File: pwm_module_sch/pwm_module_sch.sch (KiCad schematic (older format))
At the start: 47 parts, among them J1 SWIMM, J2 output -, J3 input, J4 output+, Q1 AO3400, Q2 6N60, SW1 ., SW2 ., U1 TM1637, U2 STM8S003F3P, U3 LM358, U4 L78L33

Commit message: low lewel written, not tested, todo: main menu
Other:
- moved on the sheet: C5, Q1, R4
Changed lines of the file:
@@
 L Device:R R4
 U 1 1 620AEA05
-P 4650 2800
-F 0 "R4" H 4700 2850 50  0000 L CNN
-F 1 "100k" V 4650 2700 50  0000 L CNN
-F 2 "Resistor_SMD:R_0402_1005Metric" V 4580 2800 50  0001 C CNN
-F 3 "~" H 4650 2800 50  0001 C CNN
-	1    4650 2800
-	1    0    0    -1
-$EndComp
-Wire Wire Line
-	4650 3050 4650 3000
-Connection ~ 4650 3000
-Wire Wire Line
-	4650 3000 4650 2950
+P 4700 2800
+F 0 "R4" H 4750 2850 50  0000 L CNN
+F 1 "100k" V 4700 2700 50  0000 L CNN
+F 2 "Resistor_SMD:R_0402_1005Metric" V 4630 2800 50  0001 C CNN
+F 3 "~" H 4700 2800 50  0001 C CNN
+	1    4700 2800
+	1    0    0    -1
+$EndComp
 $Comp
 L power:GND #PWR0105
@@
 	1    0    0    -1
 $EndComp
-Wire Wire Line
-	4650 3000 4950 3000
 $Comp
 L Device:R_Potentiometer RV1
@@
 	1    0    0    -1
 $EndComp
-Wire Wire Line
-	4350 2900 4350 2850
-Wire Wire Line
-	4650 2600 4650 2650
 $Comp
 L Amplifier_Operational:LM358 U3
@@
 L power:+VSW #PWR0112
 U 1 1 6218088D
-P 5200 2550
-F 0 "#PWR0112" H 5200 2400 50  0001 C CNN
-F 1 "+VSW" H 5200 2700 50  0000 C CNN
-F 2 "" H 5200 2550 50  0001 C CNN
-F 3 "" H 5200 2550 50  0001 C CNN
-	1    5200 2550
+P 5250 2550
+F 0 "#PWR0112" H 5250 2400 50  0001 C CNN
+F 1 "+VSW" H 5250 2700 50  0000 C CNN
+F 2 "" H 5250 2550 50  0001 C CNN
+F 3 "" H 5250 2550 50  0001 C CNN
+	1    5250 2550
 	1    0    0    -1
 $EndComp
@@
 L power:+24V #PWR0113
 U 1 1 6218BBB0
-P 4650 2550
-F 0 "#PWR0113" H 4650 2400 50  0001 C CNN
-F 1 "+24V" H 4650 2700 50  0000 C CNN
-F 2 "" H 4650 2550 50  0001 C CNN
-F 3 "" H 4650 2550 50  0001 C CNN
-	1    4650 2550
-	1    0    0    -1
-$EndComp
-Wire Wire Line
-	4650 2600 4650 2550
-Connection ~ 4650 2600
-Wire Wire Line
-	4750 2600 4650 2600
-Wire Wire Line
-	4950 2900 4950 3000
-Wire Wire Line
-	5150 2600 5200 2600
-Wire Wire Line
-	5200 2600 5200 2550
+P 4700 2550
+F 0 "#PWR0113" H 4700 2400 50  0001 C CNN
+F 1 "+24V" H 4700 2700 50  0000 C CNN
+F 2 "" H 4700 2550 50  0001 C CNN
+F 3 "" H 4700 2550 50  0001 C CNN
+	1    4700 2550
+	1    0    0    -1
+$EndComp
 $Comp
 L power:+3.3V #PWR0114
@@
 	1    0    0    -1
 $EndComp
-Connection ~ 5200 2600
 $Comp
 L Device:C_Polarized_US C5
 U 1 1 62166329
-P 5200 2950
-F 0 "C5" H 5200 3050 50  0000 L CNN
-F 1 "1000uF" H 4900 2850 50  0000 L CNN
-F 2 "Capacitor_THT:CP_Radial_D5.0mm_P2.00mm" H 5200 2950 50  0001 C CNN
-F 3 "~" H 5200 2950 50  0001 C CNN
-	1    5200 2950
-	1    0    0    -1
-$EndComp
-Wire Wire Line
-	5200 2800 5200 2600
+P 5250 2950
+F 0 "C5" H 5250 3050 50  0000 L CNN
+F 1 "1000uF" H 4950 2850 50  0000 L CNN
+F 2 "Capacitor_THT:CP_Radial_D5.0mm_P2.00mm" H 5250 2950 50  0001 C CNN
+F 3 "~" H 5250 2950 50  0001 C CNN
+	1    5250 2950
+	1    0    0    -1
+$EndComp
 $Comp
 L Device:R R2
@@
 Wire Wire Line
 	5300 1850 5450 1850
-Wire Wire Line
-	5450 1850 5450 2350
-Wire Wire Line
-	5450 2350 5500 2350
 Connection ~ 5300 1850
-Wire Wire Line
-	5450 2600 5450 2450
-Wire Wire Line
-	5200 2600 5450 2600
-Wire Wire Line
-	5450 2450 5500 2450
 Wire Wire Line
 	4050 1050 4100 1050
@@
 	0    1    1    0
 $EndComp
-Wire Wire Line
-	4350 3250 4350 3200
 $Comp
 L Connector_Generic:Conn_01x01 J4
@@
 L power:GND #PWR0129
 U 1 1 62235D6C
-P 5200 3550
-F 0 "#PWR0129" H 5200 3300 50  0001 C CNN
-F 1 "GND" H 5300 3450 50  0000 C CNN
-F 2 "" H 5200 3550 50  0001 C CNN
-F 3 "" H 5200 3550 50  0001 C CNN
-	1    5200 3550
+P 5250 3550
+F 0 "#PWR0129" H 5250 3300 50  0001 C CNN
+F 1 "GND" H 5350 3450 50  0000 C CNN
+F 2 "" H 5250 3550 50  0001 C CNN
+F 3 "" H 5250 3550 50  0001 C CNN
+	1    5250 3550
 	1    0    0    -1
 $EndComp
@@
 	2200 3050 2200 6250
 Wire Wire Line
-	5200 3500 5200 3100
-Wire Wire Line
 	4200 3450 4200 4650
 Wire Wire Line
-	4350 3250 4300 3250
-Wire Wire Line
 	4000 3250 3950 3250
-Wire Wire Line
-	3950 3350 4300 3350
-Wire Wire Line
-	4300 3350 4300 3900
-Connection ~ 4300 3900
-Connection ~ 4350 3250
 $Comp
 L local:AO3400 Q1
 U 1 1 620ABAF0
-P 4550 3250
-F 0 "Q1" H 4756 3296 50  0000 L CNN
-F 1 "AO3400" H 4756 3205 50  0000 L CNN
-F 2 "Package_TO_SOT_SMD:SOT-23" H 4550 3250 50  0001 C CNN
-F 3 "" H 4550 3250 50  0001 L CNN
-	1    4550 3250
-	1    0    0    -1
-$EndComp
-Wire Wire Line
-	4650 3450 4650 3500
-Wire Wire Line
-	4650 3500 5200 3500
-Wire Wire Line
-	5200 3550 5200 3500
-Connection ~ 5200 3500
+P 4600 3250
+F 0 "Q1" H 4806 3296 50  0000 L CNN
+F 1 "AO3400" H 4806 3205 50  0000 L CNN
+F 2 "Package_TO_SOT_SMD:SOT-23" H 4600 3250 50  0001 C CNN
+F 3 "" H 4600 3250 50  0001 L CNN
+	1    4600 3250
+	1    0    0    -1
+$EndComp
 $Comp
 L Device:R R11
@@
 Wire Wire Line
 	2300 5900 2300 5850
+Wire Wire Line
+	4350 3200 4350 3250
+Wire Wire Line
+	4350 3250 4400 3250
+Wire Wire Line
+	4300 3250 4350 3250
+Connection ~ 4350 3250
+Wire Wire Line
+	4350 2900 4350 2850
+Wire Wire Line
+	4700 3450 4700 3500
+Wire Wire Line
+	4950 2900 4950 3000
+Wire Wire Line
+	4950 3000 4700 3000
+Wire Wire Line
+	4700 3000 4700 3050
+Wire Wire Line
+	4700 2950 4700 3000
+Connection ~ 4700 3000
+Wire Wire Line
+	4700 2650 4700 2600
+Wire Wire Line
+	4750 2600 4700 2600
+Connection ~ 4700 2600
+Wire Wire Line
+	4700 2600 4700 2550
+Wire Wire Line
+	5150 2600 5250 2600
+Wire Wire Line
+	5250 3500 5250 3550
+Wire Wire Line
+	4700 3500 5250 3500
+Wire Wire Line
+	5250 3100 5250 3500
+Connection ~ 5250 3500
+Wire Wire Line
+	5250 2800 5250 2600
+Connection ~ 5250 2600
+Wire Wire Line
+	5250 2600 5250 2550
+Wire Wire Line
+	5450 1850 5450 2350
+Wire Wire Line
+	5450 2350 5500 2350
+Wire Wire Line
+	5250 2600 5350 2600
+Wire Wire Line
+	5350 2600 5350 2450
+Wire Wire Line
+	5350 2450 5500 2450
+Wire Wire Line
+	4300 3900 4300 3350
+Wire Wire Line
+	4300 3350 3950 3350
+Connection ~ 4300 3900
 $EndSCHEMATC

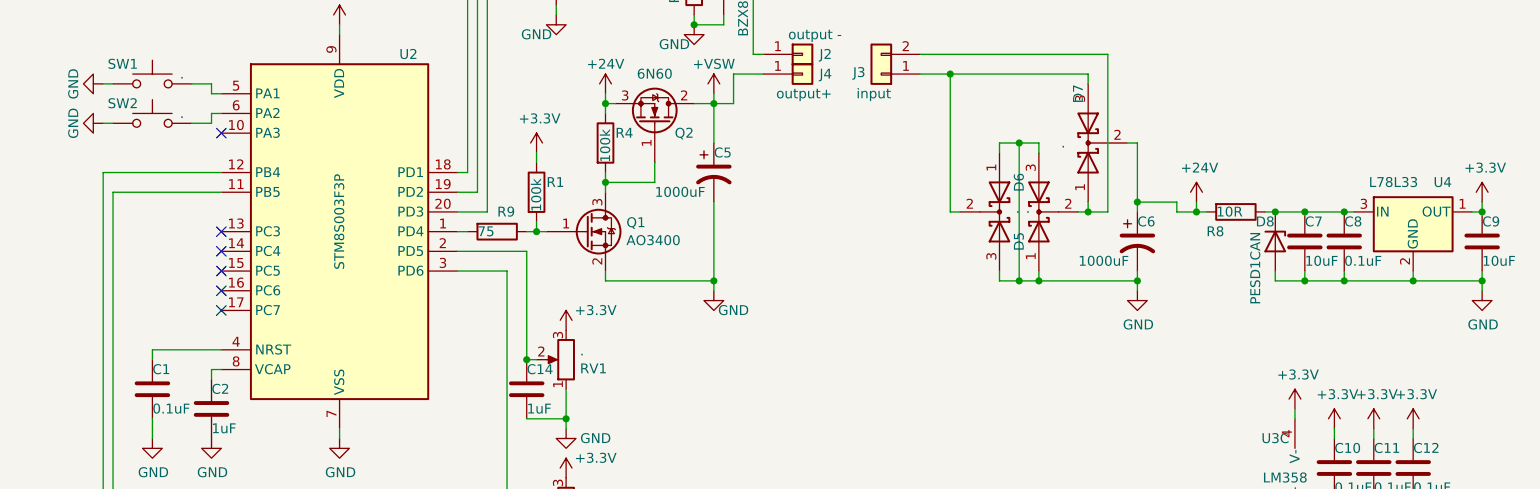
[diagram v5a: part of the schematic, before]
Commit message: uart sch add
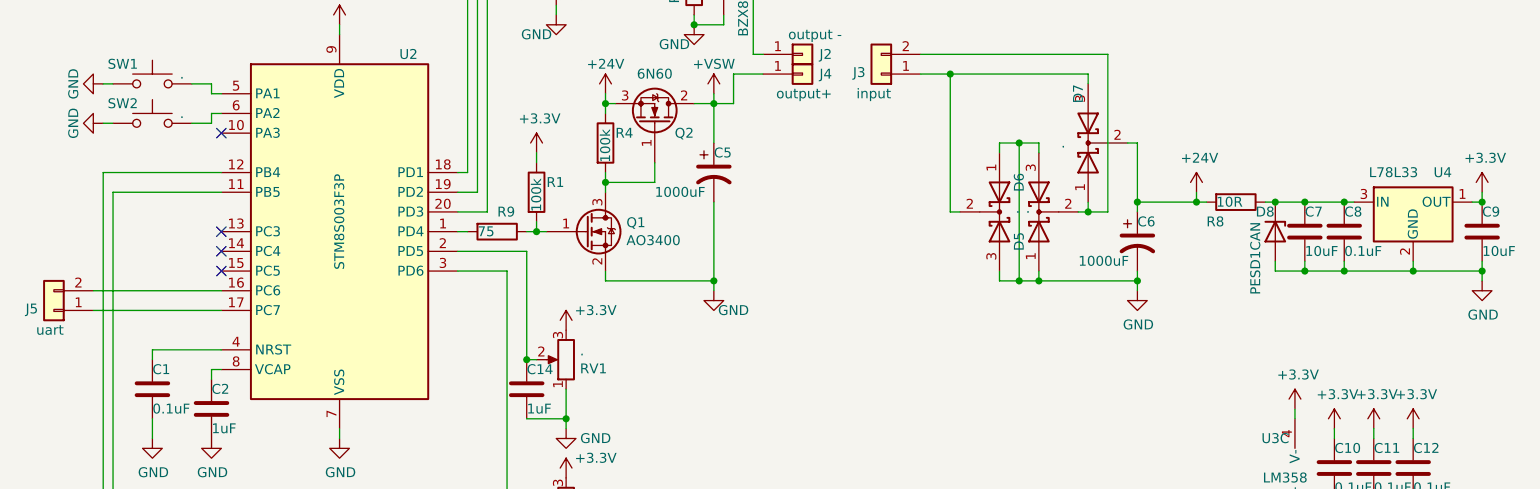
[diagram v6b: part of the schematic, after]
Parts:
- added J5: uart, Connector_PinHeader_2.54mm:PinHeader_1x02_P2.54mm_Vertical, symbol Connector_Generic:Conn_01x02
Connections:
- net at U2.16 (PC6): now also J5.2 (Pin_2)
- net at U2.17 (PC7): now also J5.1 (Pin_1)
- no-connect marks 8 -> 6
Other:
- moved on the sheet: C7, C8, C9, D8, R8, U4
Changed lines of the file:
@@
-$EndComp
-$Comp
-L Regulator_Linear:L78L33_SOT89 U4
-U 1 1 62099343
-P 8800 3150
-F 0 "U4" H 8950 3300 50  0000 C CNN
-F 1 "L78L33" H 8700 3300 50  0000 C CNN
-F 2 "Package_TO_SOT_SMD:SOT-89-3" H 8800 3350 50  0001 C CIN
-F 3 "http://www.st.com/content/ccc/resource/technical/document/datasheet/15/55/e5/aa/23/5b/43/fd/CD00000446.pdf/files/CD00000446.pdf/jcr:content/translations/en.CD00000446.pdf" H 8800 3100 50  0001 C CNN
-	1    8800 3150
-	1    0    0    -1
 $EndComp
 $Comp
 L power:+24V #PWR0108
 U 1 1 620A80C2
-P 7700 3100
-F 0 "#PWR0108" H 7700 2950 50  0001 C CNN
-F 1 "+24V" H 7715 3273 50  0000 C CNN
-F 2 "" H 7700 3100 50  0001 C CNN
-F 3 "" H 7700 3100 50  0001 C CNN
-	1    7700 3100
-	1    0    0    -1
-$EndComp
-Wire Wire Line
-	8450 3150 8500 3150
-$Comp
-L Device:C C7
-U 1 1 620AFB1A
-P 8250 3300
-F 0 "C7" H 8250 3400 50  0000 L CNN
-F 1 "10uF" H 8250 3200 50  0000 L CNN
-F 2 "Capacitor_SMD:C_0805_2012Metric" H 8288 3150 50  0001 C CNN
-F 3 "~" H 8250 3300 50  0001 C CNN
-	1    8250 3300
-	1    0    0    -1
-$EndComp
-Connection ~ 8450 3150
-$Comp
-L Device:C C8
-U 1 1 620B2675
-P 8450 3300
-F 0 "C8" H 8450 3400 50  0000 L CNN
-F 1 "0.1uF" H 8450 3200 50  0000 L CNN
-F 2 "Capacitor_SMD:C_0805_2012Metric" H 8488 3150 50  0001 C CNN
-F 3 "~" H 8450 3300 50  0001 C CNN
-	1    8450 3300
-	1    0    0    -1
-$EndComp
-Wire Wire Line
-	8450 3150 8250 3150
-$Comp
-L Device:C C9
-U 1 1 620C1410
-P 9150 3300
-F 0 "C9" H 9150 3400 50  0000 L CNN
-F 1 "10uF" H 9150 3200 50  0000 L CNN
-F 2 "Capacitor_SMD:C_0805_2012Metric" H 9188 3150 50  0001 C CNN
-F 3 "~" H 9150 3300 50  0001 C CNN
-	1    9150 3300
-	1    0    0    -1
-$EndComp
-Wire Wire Line
-	9100 3150 9150 3150
-$Comp
-L Device:R R8
-U 1 1 620CB81D
-P 7900 3150
-F 0 "R8" V 8000 3000 50  0000 L CNN
-F 1 "10R" V 7900 3050 50  0000 L CNN
-F 2 "Resistor_SMD:R_0805_2012Metric" V 7830 3150 50  0001 C CNN
-F 3 "~" H 7900 3150 50  0001 C CNN
-	1    7900 3150
-	0    1    1    0
-$EndComp
-Wire Wire Line
-	7700 3100 7700 3150
-Wire Wire Line
-	7700 3150 7750 3150
-Wire Wire Line
-	8050 3150 8100 3150
-Connection ~ 8250 3150
-Connection ~ 8100 3150
-Wire Wire Line
-	8100 3150 8250 3150
-$Comp
-L power:GND #PWR0109
-U 1 1 620E93E4
-P 9150 3550
-F 0 "#PWR0109" H 9150 3300 50  0001 C CNN
-F 1 "GND" H 9155 3377 50  0000 C CNN
-F 2 "" H 9150 3550 50  0001 C CNN
-F 3 "" H 9150 3550 50  0001 C CNN
-	1    9150 3550
-	1    0    0    -1
-$EndComp
-Wire Wire Line
-	9150 3550 9150 3500
-Wire Wire Line
-	9150 3500 8800 3500
-Wire Wire Line
-	8800 3500 8800 3450
-Connection ~ 9150 3500
-Wire Wire Line
-	9150 3500 9150 3450
-Wire Wire Line
-	8800 3500 8450 3500
-Wire Wire Line
-	8450 3500 8450 3450
-Connection ~ 8800 3500
-Wire Wire Line
-	8450 3500 8250 3500
-Wire Wire Line
-	8250 3500 8250 3450
-Connection ~ 8450 3500
-Wire Wire Line
-	8250 3500 8100 3500
-Connection ~ 8250 3500
+P 7700 3050
+F 0 "#PWR0108" H 7700 2900 50  0001 C CNN
+F 1 "+24V" H 7715 3223 50  0000 C CNN
+F 2 "" H 7700 3050 50  0001 C CNN
+F 3 "" H 7700 3050 50  0001 C CNN
+	1    7700 3050
+	1    0    0    -1
+$EndComp
+Wire Wire Line
+	7700 3050 7700 3100
+Wire Wire Line
+	7700 3100 7750 3100
 $Comp
 L power:+VSW #PWR0110
@@
 Wire Wire Line
 	2750 2950 2150 2950
-NoConn ~ 2750 3650
-NoConn ~ 2750 3550
 NoConn ~ 2750 3450
 NoConn ~ 2750 3350
@@
 $EndComp
 $Comp
-L power:+3.3V #PWR0123
-U 1 1 623818F4
-P 9150 3100
-F 0 "#PWR0123" H 9150 2950 50  0001 C CNN
-F 1 "+3.3V" H 9165 3273 50  0000 C CNN
-F 2 "" H 9150 3100 50  0001 C CNN
-F 3 "" H 9150 3100 50  0001 C CNN
-	1    9150 3100
-	1    0    0    -1
-$EndComp
-Wire Wire Line
-	9150 3150 9150 3100
-Connection ~ 9150 3150
-$Comp
 L power:+3.3V #PWR0124
 U 1 1 6238BC0F
@@
 Wire Wire Line
 	7350 2800 7400 2800
-Wire Wire Line
-	7600 3150 7700 3150
-Connection ~ 7700 3150
+Connection ~ 7700 3100
 $Comp
 L Device:C_Polarized_US C6
@@
 	7400 3550 7400 3500
 Connection ~ 7400 3500
-Wire Wire Line
-	7400 3100 7600 3100
 Connection ~ 7400 3100
 Wire Wire Line
 	7400 3100 7400 2800
-Wire Wire Line
-	7600 3100 7600 3150
 Wire Wire Line
 	2150 2500 2200 2500
@@
 $EndComp
 $Comp
-L Diode:BZX84Cxx D8
-U 1 1 6207886C
-P 8100 3300
-F 0 "D8" V 8000 3200 50  0000 L CNN
-F 1 "PESD1CAN" H 8050 3200 50  0000 L CNN
-F 2 "Diode_SMD:D_SOT-23_ANK" H 8100 3125 50  0001 C CNN
-F 3 "https://diotec.com/tl_files/diotec/files/pdf/datasheets/bzx84c2v4.pdf" H 8100 3300 50  0001 C CNN
-	1    8100 3300
-	0    1    1    0
-$EndComp
-Wire Wire Line
-	8100 3500 8100 3450
-$Comp
 L local:TM1637 U1
 U 1 1 60F48864
@@
 	4300 3350 3950 3350
 Connection ~ 4300 3900
+Wire Wire Line
+	8100 3450 8100 3400
+$Comp
+L Diode:BZX84Cxx D8
+U 1 1 6207886C
+P 8100 3250
+F 0 "D8" V 8000 3150 50  0000 L CNN
+F 1 "PESD1CAN" H 8050 3150 50  0000 L CNN
+F 2 "Diode_SMD:D_SOT-23_ANK" H 8100 3075 50  0001 C CNN
+F 3 "https://diotec.com/tl_files/diotec/files/pdf/datasheets/bzx84c2v4.pdf" H 8100 3250 50  0001 C CNN
+	1    8100 3250
+	0    1    1    0
+$EndComp
+Connection ~ 9150 3100
+Wire Wire Line
+	9150 3100 9150 3050
+$Comp
+L power:+3.3V #PWR0123
+U 1 1 623818F4
+P 9150 3050
+F 0 "#PWR0123" H 9150 2900 50  0001 C CNN
+F 1 "+3.3V" H 9165 3223 50  0000 C CNN
+F 2 "" H 9150 3050 50  0001 C CNN
+F 3 "" H 9150 3050 50  0001 C CNN
+	1    9150 3050
+	1    0    0    -1
+$EndComp
+Connection ~ 8250 3450
+Wire Wire Line
+	8250 3450 8100 3450
+Connection ~ 8450 3450
+Wire Wire Line
+	8250 3450 8250 3400
+Wire Wire Line
+	8450 3450 8250 3450
+Connection ~ 8800 3450
+Wire Wire Line
+	8450 3450 8450 3400
+Wire Wire Line
+	8800 3450 8450 3450
+Wire Wire Line
+	9150 3450 9150 3400
+Connection ~ 9150 3450
+Wire Wire Line
+	8800 3450 8800 3400
+Wire Wire Line
+	9150 3450 8800 3450
+Wire Wire Line
+	9150 3500 9150 3450
+$Comp
+L power:GND #PWR0109
+U 1 1 620E93E4
+P 9150 3500
+F 0 "#PWR0109" H 9150 3250 50  0001 C CNN
+F 1 "GND" H 9155 3327 50  0000 C CNN
+F 2 "" H 9150 3500 50  0001 C CNN
+F 3 "" H 9150 3500 50  0001 C CNN
+	1    9150 3500
+	1    0    0    -1
+$EndComp
+Wire Wire Line
+	8100 3100 8250 3100
+Connection ~ 8100 3100
+Connection ~ 8250 3100
+Wire Wire Line
+	8050 3100 8100 3100
+$Comp
+L Device:R R8
+U 1 1 620CB81D
+P 7900 3100
+F 0 "R8" V 8000 2950 50  0000 L CNN
+F 1 "10R" V 7900 3000 50  0000 L CNN
+F 2 "Resistor_SMD:R_0805_2012Metric" V 7830 3100 50  0001 C CNN
+F 3 "~" H 7900 3100 50  0001 C CNN
+	1    7900 3100
+	0    1    1    0
+$EndComp
+Wire Wire Line
+	9100 3100 9150 3100
+$Comp
+L Device:C C9
+U 1 1 620C1410
+P 9150 3250
+F 0 "C9" H 9150 3350 50  0000 L CNN
+F 1 "10uF" H 9150 3150 50  0000 L CNN
+F 2 "Capacitor_SMD:C_0805_2012Metric" H 9188 3100 50  0001 C CNN
+F 3 "~" H 9150 3250 50  0001 C CNN
+	1    9150 3250
+	1    0    0    -1
+$EndComp
+Wire Wire Line
+	8450 3100 8250 3100
+$Comp
+L Device:C C8
+U 1 1 620B2675
+P 8450 3250
+F 0 "C8" H 8450 3350 50  0000 L CNN
+F 1 "0.1uF" H 8450 3150 50  0000 L CNN
+F 2 "Capacitor_SMD:C_0805_2012Metric" H 8488 3100 50  0001 C CNN
+F 3 "~" H 8450 3250 50  0001 C CNN
+	1    8450 3250
+	1    0    0    -1
+$EndComp
+Connection ~ 8450 3100
+$Comp
+L Device:C C7
+U 1 1 620AFB1A
+P 8250 3250
+F 0 "C7" H 8250 3350 50  0000 L CNN
+F 1 "10uF" H 8250 3150 50  0000 L CNN
+F 2 "Capacitor_SMD:C_0805_2012Metric" H 8288 3100 50  0001 C CNN
+F 3 "~" H 8250 3250 50  0001 C CNN
+	1    8250 3250
+	1    0    0    -1
+$EndComp
+Wire Wire Line
+	8450 3100 8500 3100
+$Comp
+L Regulator_Linear:L78L33_SOT89 U4
+U 1 1 62099343
+P 8800 3100
+F 0 "U4" H 8950 3250 50  0000 C CNN
+F 1 "L78L33" H 8700 3250 50  0000 C CNN
+F 2 "Package_TO_SOT_SMD:SOT-89-3" H 8800 3300 50  0001 C CIN
+F 3 "http://www.st.com/content/ccc/resource/technical/document/datasheet/15/55/e5/aa/23/5b/43/fd/CD00000446.pdf/files/CD00000446.pdf/jcr:content/translations/en.CD00000446.pdf" H 8800 3050 50  0001 C CNN
+	1    8800 3100
+	1    0    0    -1
+$EndComp
+Wire Wire Line
+	7400 3100 7700 3100
+$Comp
+L Connector_Generic:Conn_01x02 J5
+U 1 1 621F9B6F
+P 1900 3650
+F 0 "J5" H 1980 3642 50  0000 L CNN
+F 1 "uart" H 1850 3750 50  0000 L CNN
+F 2 "Connector_PinHeader_2.54mm:PinHeader_1x02_P2.54mm_Vertical" H 1900 3650 50  0001 C CNN
+F 3 "~" H 1900 3650 50  0001 C CNN
+	1    1900 3650
+	-1   0    0    1
+$EndComp
+Wire Wire Line
+	2750 3550 2100 3550
+Wire Wire Line
+	2100 3650 2750 3650
 $EndSCHEMATC

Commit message: reduced dimentions
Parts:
- added R12: 10k, Resistor_SMD:R_1210_3225Metric, symbol Device:R
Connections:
- net +VSW: now also R12.2
- net GND: now also R12.1
- net at U2.19 (PD2): now also R3.2; no longer R2.2
- net at U2.20 (PD3): now also R2.2; no longer R3.2
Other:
- moved on the sheet: C3, C4, C5, D3, D4, J1, J5, R2, R3, R5, R6, R7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

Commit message: 0402 caps
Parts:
- C1, C10, C11, C12, C3, C4: footprint Capacitor_SMD:C_0805_2012Metric -> Capacitor_SMD:C_0402_1005Metric
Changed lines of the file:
@@
 F 0 "C1" H 2400 4150 50  0000 L CNN
 F 1 "0.1uF" H 2400 3950 50  0000 L CNN
-F 2 "Capacitor_SMD:C_0805_2012Metric" H 2438 3900 50  0001 C CNN
+F 2 "Capacitor_SMD:C_0402_1005Metric" H 2438 3900 50  0001 C CNN
 F 3 "~" H 2400 4050 50  0001 C CNN
 	1    2400 4050
@@
 F 0 "C10" H 8400 4550 50  0000 L CNN
 F 1 "0.1uF" H 8400 4350 50  0000 L CNN
-F 2 "Capacitor_SMD:C_0805_2012Metric" H 8438 4300 50  0001 C CNN
+F 2 "Capacitor_SMD:C_0402_1005Metric" H 8438 4300 50  0001 C CNN
 F 3 "~" H 8400 4450 50  0001 C CNN
 	1    8400 4450
@@
 F 0 "C11" H 8600 4550 50  0000 L CNN
 F 1 "0.1uF" H 8600 4350 50  0000 L CNN
-F 2 "Capacitor_SMD:C_0805_2012Metric" H 8638 4300 50  0001 C CNN
+F 2 "Capacitor_SMD:C_0402_1005Metric" H 8638 4300 50  0001 C CNN
 F 3 "~" H 8600 4450 50  0001 C CNN
 	1    8600 4450
@@
 F 0 "C12" H 8800 4550 50  0000 L CNN
 F 1 "0.1uF" H 8800 4350 50  0000 L CNN
-F 2 "Capacitor_SMD:C_0805_2012Metric" H 8838 4300 50  0001 C CNN
+F 2 "Capacitor_SMD:C_0402_1005Metric" H 8838 4300 50  0001 C CNN
 F 3 "~" H 8800 4450 50  0001 C CNN
 	1    8800 4450
@@
 F 0 "C4" H 4400 1100 50  0000 L CNN
 F 1 "0.1uF" H 4400 900 50  0000 L CNN
-F 2 "Capacitor_SMD:C_0805_2012Metric" H 4438 850 50  0001 C CNN
+F 2 "Capacitor_SMD:C_0402_1005Metric" H 4438 850 50  0001 C CNN
 F 3 "~" H 4400 1000 50  0001 C CNN
 	1    4400 1000
@@
 F 0 "C3" H 4500 2050 50  0000 L CNN
 F 1 "0.1uF" H 4500 1850 50  0000 L CNN
-F 2 "Capacitor_SMD:C_0805_2012Metric" H 4538 1800 50  0001 C CNN
+F 2 "Capacitor_SMD:C_0402_1005Metric" H 4538 1800 50  0001 C CNN
 F 3 "~" H 4500 1950 50  0001 C CNN
 	1    4500 1950
